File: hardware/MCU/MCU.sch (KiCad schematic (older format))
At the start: 41 parts, among them P1 CONN_01X05, P2 CONN_01X04, P3 CONN_01X05, U1 MAX6369, U2 DS18B20, U3 TC1262-30VDB, U4 PIC18F45K22, U5 LT6005, Y1 Crystal

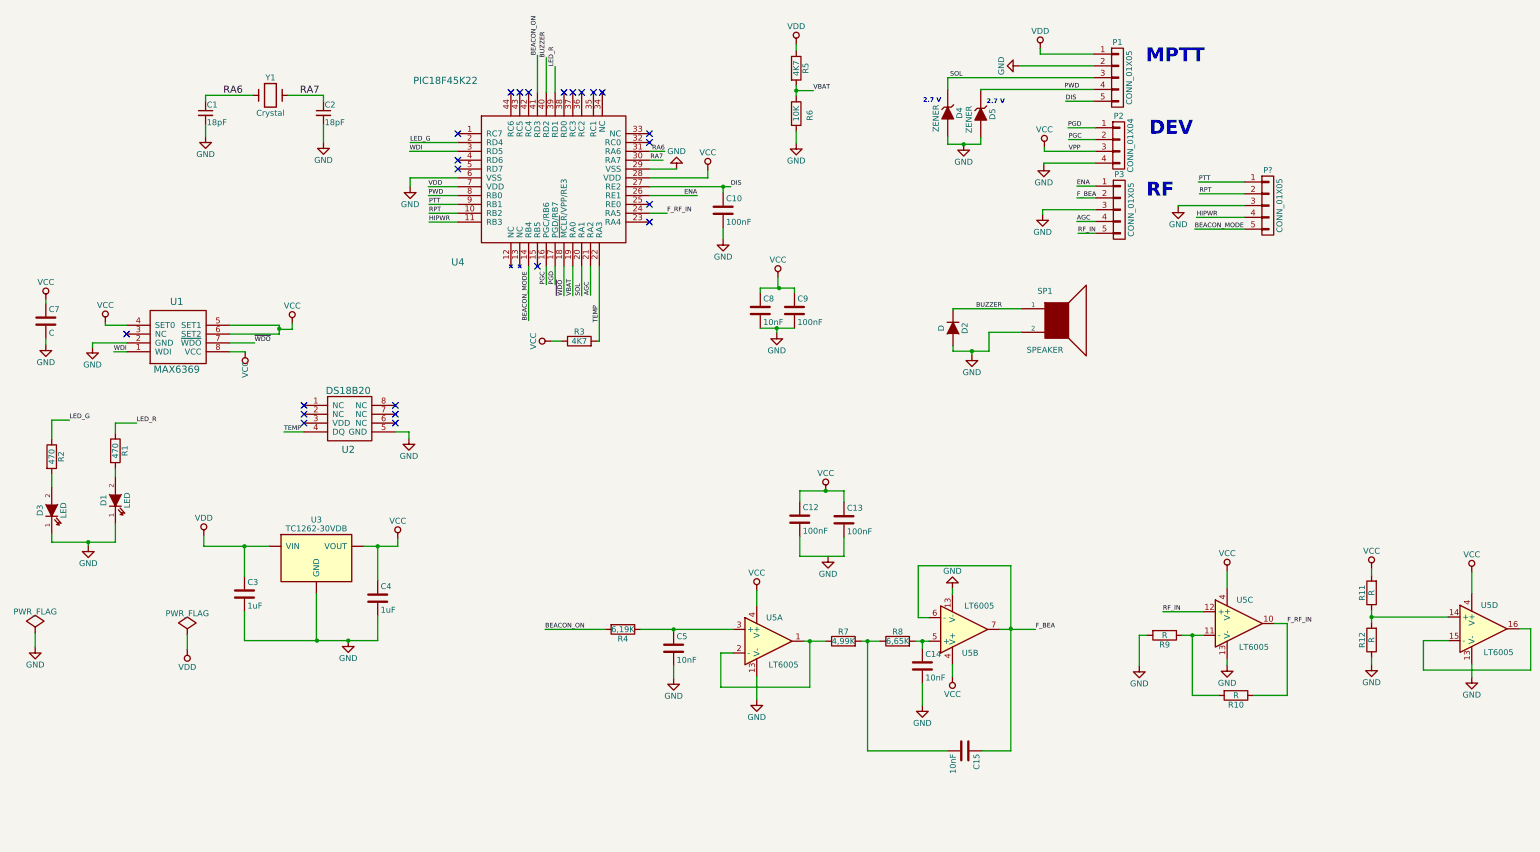
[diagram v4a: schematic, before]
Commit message: Modificaciones para fabricación:   - Añadidos campos en los componentes (esquemáticos).   - Añadida carpeta Documentos/Montador/   - Creada primera versión del BOM (formato HTML, CSV y XML).
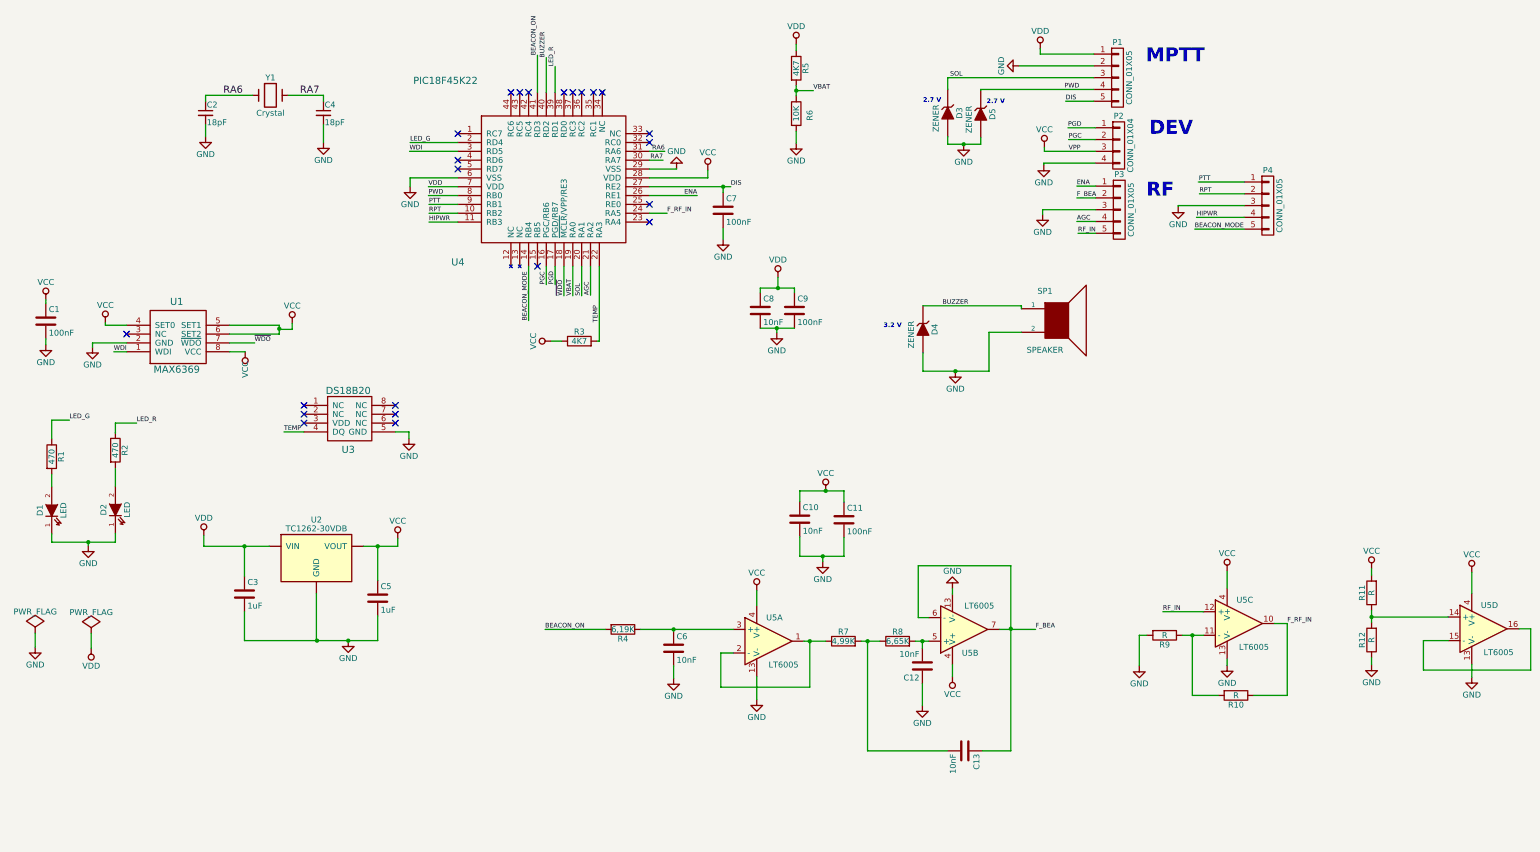
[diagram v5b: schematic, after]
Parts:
- removed C14, C15: 10nF, Capacitors_SMD:C_0603_HandSoldering, symbol C
- removed C2: 18pF, Capacitors_SMD:C_0603_HandSoldering, symbol C_Small
- removed C4: 1uF, Capacitors_SMD:C_0603_HandSoldering, symbol C
- removed D2: D, Diodes_SMD:D_SOD-523, symbol D
- removed P?: CONN_01X05, Sockets_MOLEX_KK-System:Socket_MOLEX-KK-RM2-54mm_Lock_4pin_straight, symbol CONN_01X05
- removed R1: 470, Resistors_SMD:R_0603_HandSoldering, symbol R
- added C11, C7: 100nF, Capacitors_SMD:C_0603_HandSoldering, symbol C
- added C4: 18pF, Capacitors_SMD:C_0603_HandSoldering, symbol C_Small
- added C6: 10nF, Capacitors_SMD:C_0603_HandSoldering, symbol C
- added D4: ZENER, Diodes_SMD:D_SOD-323_HandSoldering, symbol ZENER
- added P4: CONN_01X05, Connectors_Terminal_Blocks:TerminalBlock_Pheonix_MPT-2.54mm_5pol, symbol CONN_01X05
- added R2: 470, Resistors_SMD:R_0603_HandSoldering, symbol R
- C1: renamed from C7; value C -> 100nF; Descripción (none) -> Condensador de Cerámica Multicapa, Terminación Flexible (FT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; Fabricante (none) -> KEMET; Proveedor #1 (none) -> Mouser; Proveedor #2 (none) -> Farnell; Referencia Fabricante (none) -> 80-C0603X104K5R; Referencia Proveedor #1 (none) -> C0603X104K5RACTU; Referencia Proveedor #2 (none) -> 1414028
- C10, C12, C13: value 100nF -> 10nF; Descripción (none) -> Ceramic Capacitors MLCC - SMD/SMT 50volts 10000pF 1% U2J; Fabricante (none) -> KEMET; Proveedor #1 (none) -> Mouser; Proveedor #2 (none) -> Farnell; Referencia Fabricante (none) -> C0603X103F5JACTU; Referencia Proveedor #1 (none) -> 80-C0603X103F5J; Referencia Proveedor #2 (none) -> 2579110
- C2: renamed from C1; Descripción (none) -> Multilayer Ceramic Capacitors MLCC - SMD/SMT 250volts 18pF 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; Fabricante (none) -> KEMET; Proveedor #1 (none) -> Mouser; Proveedor #2 (none) -> Farnell; Referencia Fabricante (none) -> CBR06C180FAGAC; Referencia Proveedor #1 (none) -> 80-CBR06C180FAGAC; Referencia Proveedor #2 (none) -> -
- C3: Descripción (none) -> TDK C0603X5R0J105M030BC Condensador de Cerámica Multicapa, 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; Fabricante (none) -> TDK; Proveedor #1 (none) -> Mouser; Proveedor #2 (none) -> Farnell; Referencia Fabricante (none) -> C0603X5R0J105M030BC; Referencia Proveedor #1 (none) -> 810-C0603X5R0J105M; Referencia Proveedor #2 (none) -> 2524945
- C5: value 10nF -> 1uF; Descripción (none) -> TDK C0603X5R0J105M030BC Condensador de Cerámica Multicapa, 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; Fabricante (none) -> TDK; Proveedor #1 (none) -> Mouser; Proveedor #2 (none) -> Farnell; Referencia Fabricante (none) -> C0603X5R0J105M030BC; Referencia Proveedor #1 (none) -> 810-C0603X5R0J105M; Referencia Proveedor #2 (none) -> 2524945
- C8: Descripción (none) -> Ceramic Capacitors MLCC - SMD/SMT 50volts 10000pF 1% U2J; Fabricante (none) -> KEMET; Proveedor #1 (none) -> Mouser; Proveedor #2 (none) -> Farnell; Referencia Fabricante (none) -> C0603X103F5JACTU; Referencia Proveedor #1 (none) -> 80-C0603X103F5J; Referencia Proveedor #2 (none) -> 2579110
- C9: Descripción (none) -> Condensador de Cerámica Multicapa, Terminación Flexible (FT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; Fabricante (none) -> KEMET; Proveedor #1 (none) -> Mouser; Proveedor #2 (none) -> Farnell; Referencia Fabricante (none) -> 80-C0603X104K5R; Referencia Proveedor #1 (none) -> C0603X104K5RACTU; Referencia Proveedor #2 (none) -> 1414028
- D1: renamed from D3; Fabricante (none) -> VISHAY; Proveedor #1 (none) -> Mouser; Proveedor #2 (none) -> Farnell; Referencia Fabricante (none) -> VLMTG1300-GS08; Referencia Proveedor #1 (none) -> VLMTG1300-GS08; Referencia Proveedor #2 (none) -> 2251490
- D2: renamed from D1; Fabricante (none) -> VISHAY; Proveedor #1 (none) -> Mouser; Proveedor #2 (none) -> Farnell; Referencia Fabricante (none) -> VLMS1300-GS08; Referencia Proveedor #1 (none) -> 78-VLMS1300-GS08; Referencia Proveedor #2 (none) -> 2251484
- D3: renamed from D4; Descripción (none) -> Diodo Zener Simple, Regulador de Tensión, 2.7 V, 500 mW, SO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; Fabricante (none) -> ON SEMICONDUCTOR; Proveedor #1 (none) -> Mouser; Proveedor #2 (none) -> Farnell; Referencia Fabricante (none) -> MMSZ5223BT1G; Referencia Proveedor #1 (none) -> 863-MMSZ5223BT1G; Referencia Proveedor #2 (none) -> 2463576
- D5: Descripción (none) -> Diodo Zener Simple, Regulador de Tensión, 2.7 V, 500 mW, SO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; Fabricante (none) -> ON SEMICONDUCTOR; Proveedor #1 (none) -> Mouser; Proveedor #2 (none) -> Farnell; Referencia Fabricante (none) -> MMSZ5223BT1G; Referencia Proveedor #1 (none) -> 863-MMSZ5223BT1G; Referencia Proveedor #2 (none) -> 2463576
- P1: footprint Sockets_MOLEX_KK-System:Socket_MOLEX-KK-RM2-54mm_Lock_5pin_straight -> Connectors_Terminal_Blocks:TerminalBlock_Pheonix_MPT-2.54mm_5pol; Descripción (none) -> Conector de Placa a Placa, 2.54 mm, 5 Contactos, Receptácul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; Fabricante (none) -> 3M; Proveedor #1 (none) -> Mouser; Proveedor #2 (none) -> Farnell; Referencia Fabricante (none) -> 960105-6202-AR; Referencia Proveedor #1 (none) -> 517-9601056202AR; Referencia Proveedor #2 (none) -> 2672610
- P2: Descripción (none) -> Conector de Placa a Placa, 2.54 mm, 4 Contactos, Receptácul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; Fabricante (none) -> 3M; Proveedor #1 (none) -> Mouser; Proveedor #2 (none) -> Farnell; Referencia Fabricante (none) -> 960104-6202-AR; Referencia Proveedor #1 (none) -> 517-9601046202AR; Referencia Proveedor #2 (none) -> 2672609
- P3: footprint Sockets_MOLEX_KK-System:Socket_MOLEX-KK-RM2-54mm_Lock_4pin_straight -> Connectors_Terminal_Blocks:TerminalBlock_Pheonix_MPT-2.54mm_5pol; Descripción (none) -> Conector de Placa a Placa, 2.54 mm, 5 Contactos, Receptácul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; Fabricante (none) -> 3M; Proveedor #1 (none) -> Mouser; Proveedor #2 (none) -> Farnell; Referencia Fabricante (none) -> 960105-6202-AR; Referencia Proveedor #1 (none) -> 517-9601056202AR; Referencia Proveedor #2 (none) -> 2672610
- R1: renamed from R2; Fabricante (none) -> YAGEO; Proveedor #1 (none) -> Mouser; Proveedor #2 (none) -> Farnell; Referencia Fabricante (none) -> RT0603FRE07470RL; Referencia Proveedor #1 (none) -> 603-RT0603FRE07470RL; Referencia Proveedor #2 (none) -> 1500635
- R3, R5: Descripción (none) -> TNPW06034K75BEEA RES, THIN FILM, 4K75, 0.1%, 0.063W, 0603; Fabricante (none) -> VISHAY; Proveedor #1 (none) -> Mouser; Proveedor #2 (none) -> Farnell; Referencia Fabricante (none) -> TNPW06034K75BEEA; Referencia Proveedor #1 (none) -> 71-TNPW06034K75BEEA; Referencia Proveedor #2 (none) -> 1893941
- R4: Descripción (none) -> 1160352; Fabricante (none) -> WELWYN; Proveedor #1 (none) -> Mouser; Proveedor #2 (none) -> Farnell; Referencia Fabricante (none) -> PCF0603R-6K19BT1; Referencia Proveedor #1 (none) -> 756-PCF0603R-6K19BT1; Referencia Proveedor #2 (none) -> Farnell
- R6: Descripción (none) -> Resistencia SMD de Tipo Chip, Película Gruesa, 10 kohm, 75 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; Fabricante (none) -> Value; Proveedor #1 (none) -> Mouser; Proveedor #2 (none) -> Farnell; Referencia Fabricante (none) -> Value; Referencia Proveedor #1 (none) -> 71-CRCW0603-10K-E3; Referencia Proveedor #2 (none) -> 1469748
- R7: Descripción (none) -> Resistencia SMD de Tipo Chip, Película Gruesa, 4.99 kohm, 7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; Fabricante (none) -> PANASONIC; Proveedor #1 (none) -> Mouser; Proveedor #2 (none) -> Farnell; Referencia Fabricante (none) -> ERJ-3EKF4991V; Referencia Proveedor #1 (none) -> 667-ERJ-3EKF4991V; Referencia Proveedor #2 (none) -> 2059377
- R8: Descripción (none) -> Resistencia SMD de Tipo Chip, Película Delgada, 6.65 kohm, 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; Fabricante (none) -> VISHAY; Proveedor #1 (none) -> Mouser; Proveedor #2 (none) -> Farnell; Referencia Fabricante (none) -> TNPW06036K65BEEA; Referencia Proveedor #1 (none) -> 71-TNPW06036K65BEEA; Referencia Proveedor #2 (none) -> 1809818
- U1: Descripción (none) -> Supervisory Circuits Pin-Selectable Watchdog Timer; MAXIM (none) -> Value; Proveedor #1 (none) -> Mouser; Proveedor #2 (none) -> Farnell; Referencia Fabricante (none) -> MAX6369KA+T; Referencia Proveedor #1 (none) -> 700-MAX6369KAT; Referencia Proveedor #2 (none) -> 2519138
- U2: renamed from U3; Descripción (none) -> MICROCHIP TC1262-3.0VDB Regulador de Tensión Fija LDO, 2.7V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; Fabricante (none) -> MICROCHIP; Proveedor #1 (none) -> Mouser; Proveedor #2 (none) -> Farnell; Referencia Fabricante (none) -> TC1262-3.VBD; Referencia Proveedor #1 (none) -> 579-TC1262-3.0VDB; Referencia Proveedor #2 (none) -> 1852181
- U3: renamed from U2; footprint Housings_SOIC:SOIC-8_3.9x4.9mm_Pitch1.27mm -> Housings_SSOP:MSOP-8_3x3mm_Pitch0.65mm; Descripción (none) -> MAXIM INTEGRATED PRODUCTS DS18B20U+ IC de Detección de Temp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; MAXIM INTEGRATED (none) -> Value; Proveedor #1 (none) -> Mouser; Proveedor #2 (none) -> Farnell; Referencia Fabricante (none) -> DS18B20U+; Referencia Proveedor #1 (none) -> 700-DS18B20U; Referencia Proveedor #2 (none) -> 2518694
- U4: Descripción (none) -> 8-bit Microcontrollers - MCU 32KB Flash 1536B RAM 8B nanoWa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; Fabricante (none) -> MICROCHIP; Proveedor #1 (none) -> Mouser; Proveedor #2 (none) -> Farnell; Referencia Fabricante (none) -> PIC18F45K22-I/PT; Referencia Proveedor #1 (none) -> 579-PIC18F45K22-I/PT; Referencia Proveedor #2 (none) -> 1840995
- U5: Descripción (none) -> Amplificador Operacional, Cuádruple, 4 Amplificadores, 2 kH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; Fabricante (none) -> LINEAR TECHNOLOGY; Proveedor #1 (none) -> Mouser; Proveedor #2 (none) -> Farnell; Referencia Fabricante (none) -> LT6005IGN#PBF; Referencia Proveedor #1 (none) -> -; Referencia Proveedor #2 (none) -> 1432099
- Y1: Descripción (none) -> Cristal, 20 MHz, Agujero Pasante, 11.5mm x 5mm, 100 ppm, 18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; Fabricante (none) -> ABRACON; Proveedor #1 (none) -> Mouser; Proveedor #2 (none) -> Farnell; Referencia Fabricante (none) -> AB-2.000MHZ-B2; Referencia Proveedor #1 (none) -> 815-AB-2-B2; Referencia Proveedor #2 (none) -> 1611769
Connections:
- net BEACON_MODE: now also P4.5 (P5)
- net BUZZER: now also D4.1 (K)
- net DIS: now also C7.1; no longer C10.1
- net GND: now also C12.1, C11.2, C4.2, C6.2, C7.2, D4.2 (A), P4.3 (P3)
- net HIPWR: now also P4.4 (P4)
- net PTT: now also P4.1 (P1)
- net RA7: now also C4.1
- net RPT: now also P4.2 (P2)
- net VCC: now also C10.1, C5.1, C11.1; no longer C12.1, C13.1, C8.1, C9.1
- net VDD: now also C8.1, C9.1
- net at C13.2: now also R7.2, R8.1; no longer C12.2
- net at R4.1, U5.3 (+): now also C6.1; no longer C5.1
- net at R8.2, U5.5 (+): now also C12.2
- net at U5.6 (-): now also C13.1
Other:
- note added: "3.2 V"
- moved on the sheet: D2

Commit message: MCU: Añadidos ficheros de fabricacion. Lista para fabricar la versión 1.0 a falta de retoques de serigrafía (logo)
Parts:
- added FID1, FID2, FID3: FIDUCIAL, Fiducials:Fiducial_1mm_Dia_2.54mm_Outer_CopperTop, symbol FIDUCIAL
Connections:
- net LED_R: now also R2.1
- net at D2.2 (A): now also R2.2
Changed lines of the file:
@@
 LIBS:max6369
 LIBS:MCU-Components
+LIBS:mechanical
+LIBS:fiducial
 LIBS:MCU-cache
 EELAYER 25 0
@@
 encoding utf-8
 Sheet 1 1
-Title ""
-Date ""
-Rev ""
-Comp ""
+Title "EASAT MCU"
+Date "2017-05-15"
+Rev "1.0"
+Comp "EASAT"
 Comment1 ""
 Comment2 ""
@@
 	9160 3235 8885 3235
 Wire Wire Line
-	8885 3235 8885 3565
+	8885 3565 8885 3235
 Wire Wire Line
 	2445 3325 2656 3325
@@
 	5355 2675 5355 2925
 Wire Wire Line
-	7250 1230 7250 1145
+	7250 1145 7250 1230
 Wire Wire Line
 	7250 1530 7250 1630
@@
 	6210 6065 6210 6170
 Wire Wire Line
-	7500 5855 7315 5855
+	7315 5855 7500 5855
 Wire Wire Line
 	7365 6245 7365 5855
@@
 $EndComp
 Wire Wire Line
-	8885 3565 8325 3565
+	8325 3565 8885 3565
 Wire Wire Line
 	8325 3565 8325 3410
@@
 L R R2
 U 1 1 59041535
-P 1475 4235
-F 0 "R2" V 1555 4235 50  0000 C CNN
-F 1 "470" V 1475 4235 50  0000 C CNN
-F 2 "Resistors_SMD:R_0603_HandSoldering" H 1405 4235 50  0001 C CNN
-F 3 "" H 1475 4235 50  0000 C CNN
-F 4 "YAGEO" H 1475 4235 60  0001 C CNN "Fabricante"
-F 5 "RT0603FRE07470RL" H 1475 4235 60  0001 C CNN "Referencia Fabricante"
-F 6 "Mouser" H 1475 4235 60  0001 C CNN "Proveedor #1"
-F 7 "603-RT0603FRE07470RL" H 1475 4235 60  0001 C CNN "Referencia Proveedor #1"
-F 8 "Farnell" H 1475 4235 60  0001 C CNN "Proveedor #2"
-F 9 "1500635" H 1475 4235 60  0001 C CNN "Referencia Proveedor #2"
-	1    1475 4235
+P 1475 4240
+F 0 "R2" V 1555 4240 50  0000 C CNN
+F 1 "470" V 1475 4240 50  0000 C CNN
+F 2 "Resistors_SMD:R_0603_HandSoldering" H 1405 4240 50  0001 C CNN
+F 3 "" H 1475 4240 50  0000 C CNN
+F 4 "YAGEO" H 1475 4240 60  0001 C CNN "Fabricante"
+F 5 "RT0603FRE07470RL" H 1475 4240 60  0001 C CNN "Referencia Fabricante"
+F 6 "Mouser" H 1475 4240 60  0001 C CNN "Proveedor #1"
+F 7 "603-RT0603FRE07470RL" H 1475 4240 60  0001 C CNN "Referencia Proveedor #1"
+F 8 "Farnell" H 1475 4240 60  0001 C CNN "Proveedor #2"
+F 9 "1500635" H 1475 4240 60  0001 C CNN "Referencia Proveedor #2"
+	1    1475 4240
 	1    0    0    -1
 $EndComp
@@
 	1    0    0    -1
 $EndComp
+$Comp
+L FIDUCIAL FID1
+U 1 1 591A5C55
+P 11790 1035
+F 0 "FID1" H 11790 1160 60  0000 C CNN
+F 1 "FIDUCIAL" H 11790 910 60  0000 C CNN
+F 2 "Fiducials:Fiducial_1mm_Dia_2.54mm_Outer_CopperTop" H 11790 1035 60  0001 C CNN
+F 3 "" H 11790 1035 60  0000 C CNN
+	1    11790 1035
+	1    0    0    -1
+$EndComp
+$Comp
+L FIDUCIAL FID2
+U 1 1 591A6223
+P 12190 1035
+F 0 "FID2" H 12190 1160 60  0000 C CNN
+F 1 "FIDUCIAL" H 12190 910 60  0000 C CNN
+F 2 "Fiducials:Fiducial_1mm_Dia_2.54mm_Outer_CopperTop" H 12190 1035 60  0001 C CNN
+F 3 "" H 12190 1035 60  0000 C CNN
+	1    12190 1035
+	1    0    0    -1
+$EndComp
+$Comp
+L FIDUCIAL FID3
+U 1 1 591A629A
+P 12605 1035
+F 0 "FID3" H 12605 1160 60  0000 C CNN
+F 1 "FIDUCIAL" H 12605 910 60  0000 C CNN
+F 2 "Fiducials:Fiducial_1mm_Dia_2.54mm_Outer_CopperTop" H 12605 1035 60  0001 C CNN
+F 3 "" H 12605 1035 60  0000 C CNN
+	1    12605 1035
+	1    0    0    -1
+$EndComp

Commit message: MCU Version 1.0 lista para fabricación. Ficheros generados.
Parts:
- added R13: 10K, Resistors_SMD:R_0603_HandSoldering, symbol R
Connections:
- net DIS: no longer U4.27 (RE2)
- net GND: no longer C7.2
- net VCC: now also R13.1
- net ~WDO: now also R13.2
- new net: C7.2, U4.27 (RE2)
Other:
- moved on the sheet: C7

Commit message: - Esquematicos generados - Archivos de fabricacion - BOM para Farnell
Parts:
- R10: Fabricante (none) -> PANASONIC; Proveedor #1 (none) -> Farnell; Proveedor #2 (none) -> Mouser; Referencia Fabricante (none) -> ERJ3EKF2002V; Referencia Proveedor #1 (none) -> 2059432; Referencia Proveedor #2 (none) -> 667-ERJ-3EKF2002V
- R11, R9: value R -> 1K;  Proveedor #1 (none) -> Farnell; Fabricante (none) -> WELWYN; Referencia Fabricante (none) -> WCR0603-1K0FI; Referencia Proveedor #1 (none) -> 2422029
- R12: value R -> 1K;  Proveedor #2 (none) -> Farnell; Fabricante (none) -> WELWYN; Proveedor #1 (none) -> Mouser; Referencia Fabricante (none) -> WCR0603-1K0FI; Referencia Proveedor #2 (none) -> 2422029
- SP1: Fabricante (none) -> PRO SIGNAL; Proveedor #1 (none) -> Farnell; Referencia Fabricante (none) -> ABI-050-RC; Referencia Proveedor #1 (none) -> 2534976
- U1: Fabricante (none) -> MAXIM
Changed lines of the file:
@@
 F 9 "2519138" H 1995 3050 60  0001 C CNN "Referencia Proveedor #2"
 F 10 "Supervisory Circuits Pin-Selectable Watchdog Timer" H 1995 3050 60  0001 C CNN "Descripción"
+F 11 "MAXIM" H 1995 3050 60  0001 C CNN "Fabricante"
 	1    1995 3050
 	1    0    0    1
@@
 F 2 "Buzzers_Beepers:MagneticBuzzer_Kingstate_KCG0601" H 9460 3135 50  0001 C CNN
 F 3 "" H 9460 3135 50  0000 C CNN
+F 4 "PRO SIGNAL" H 9460 3135 60  0001 C CNN "Fabricante"
+F 5 "ABI-050-RC" H 9460 3135 60  0001 C CNN "Referencia Fabricante"
+F 6 "Farnell" H 9460 3135 60  0001 C CNN "Proveedor #1"
+F 7 "2534976" H 9460 3135 60  0001 C CNN "Referencia Proveedor #1"
 	1    9460 3135
 	1    0    0    -1
@@
 P 10375 5805
 F 0 "R9" V 10455 5805 50  0000 C CNN
-F 1 "R" V 10375 5805 50  0000 C CNN
+F 1 "1K" V 10375 5805 50  0000 C CNN
 F 2 "Resistors_SMD:R_0603_HandSoldering" V 10305 5805 50  0001 C CNN
 F 3 "" H 10375 5805 50  0000 C CNN
+F 4 "WELWYN" V 10375 5805 60  0001 C CNN "Fabricante"
+F 5 "WCR0603-1K0FI" V 10375 5805 60  0001 C CNN "Referencia Fabricante"
+F 6 "Farnell" V 10375 5805 60  0001 C CNN " Proveedor #1"
+F 7 "2422029" V 10375 5805 60  0001 C CNN "Referencia Proveedor #1"
 	1    10375 5805
 	0    1    1    0
@@
 F 2 "Resistors_SMD:R_0603_HandSoldering" V 10910 6315 50  0001 C CNN
 F 3 "" H 10980 6315 50  0000 C CNN
+F 4 "PANASONIC" V 10980 6315 60  0001 C CNN "Fabricante"
+F 5 "ERJ3EKF2002V" V 10980 6315 60  0001 C CNN "Referencia Fabricante"
+F 6 "Farnell" V 10980 6315 60  0001 C CNN "Proveedor #1"
+F 7 "Mouser" V 10980 6315 60  0001 C CNN "Proveedor #2"
+F 8 "2059432" V 10980 6315 60  0001 C CNN "Referencia Proveedor #1"
+F 9 "667-ERJ-3EKF2002V" V 10980 6315 60  0001 C CNN "Referencia Proveedor #2"
 	1    10980 6315
 	0    1    1    0
@@
 $EndComp
 $Comp
-L R R11
-U 1 1 58C78986
-P 12130 5445
-F 0 "R11" V 12210 5445 50  0000 C CNN
-F 1 "R" V 12130 5445 50  0000 C CNN
-F 2 "Resistors_SMD:R_0603_HandSoldering" V 12060 5445 50  0001 C CNN
-F 3 "" H 12130 5445 50  0000 C CNN
-	1    12130 5445
-	-1   0    0    1
-$EndComp
-$Comp
 L R R12
 U 1 1 58C78BAD
 P 12130 5845
 F 0 "R12" V 12210 5845 50  0000 C CNN
-F 1 "R" V 12130 5845 50  0000 C CNN
+F 1 "1K" V 12130 5845 50  0000 C CNN
 F 2 "Resistors_SMD:R_0603_HandSoldering" V 12060 5845 50  0001 C CNN
 F 3 "" H 12130 5845 50  0000 C CNN
+F 4 "WCR0603-1K0FI" V 12130 5845 60  0001 C CNN "Referencia Fabricante"
+F 5 "WELWYN" V 12130 5845 60  0001 C CNN "Fabricante"
+F 6 "Mouser" V 12130 5845 60  0001 C CNN "Proveedor #1"
+F 7 "Farnell" V 12130 5845 60  0001 C CNN " Proveedor #2"
+F 8 "2422029" V 12130 5845 60  0001 C CNN "Referencia Proveedor #2"
 	1    12130 5845
 	-1   0    0    1
@@
 	3170 2985 3175 2985
 Connection ~ 3175 2985
+$Comp
+L R R11
+U 1 1 58C78986
+P 12130 5445
+F 0 "R11" V 12210 5445 50  0000 C CNN
+F 1 "1K" V 12130 5445 50  0000 C CNN
+F 2 "Resistors_SMD:R_0603_HandSoldering" V 12060 5445 50  0001 C CNN
+F 3 "" H 12130 5445 50  0000 C CNN
+F 4 "WELWYN" V 12130 5445 60  0001 C CNN "Fabricante"
+F 5 "WCR0603-1K0FI" V 12130 5445 60  0001 C CNN "Referencia Fabricante"
+F 6 "Farnell" V 12130 5445 60  0001 C CNN " Proveedor #1"
+F 7 "2422029" V 12130 5445 60  0001 C CNN "Referencia Proveedor #1"
+	1    12130 5445
+	-1   0    0    1
+$EndComp
 $EndSCHEMATC
